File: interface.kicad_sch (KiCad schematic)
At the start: 11 parts, among them J2 USB_C_Receptacle_USB2.0_16P, U2 USBLC6-2P6, U3 FT230XS-R

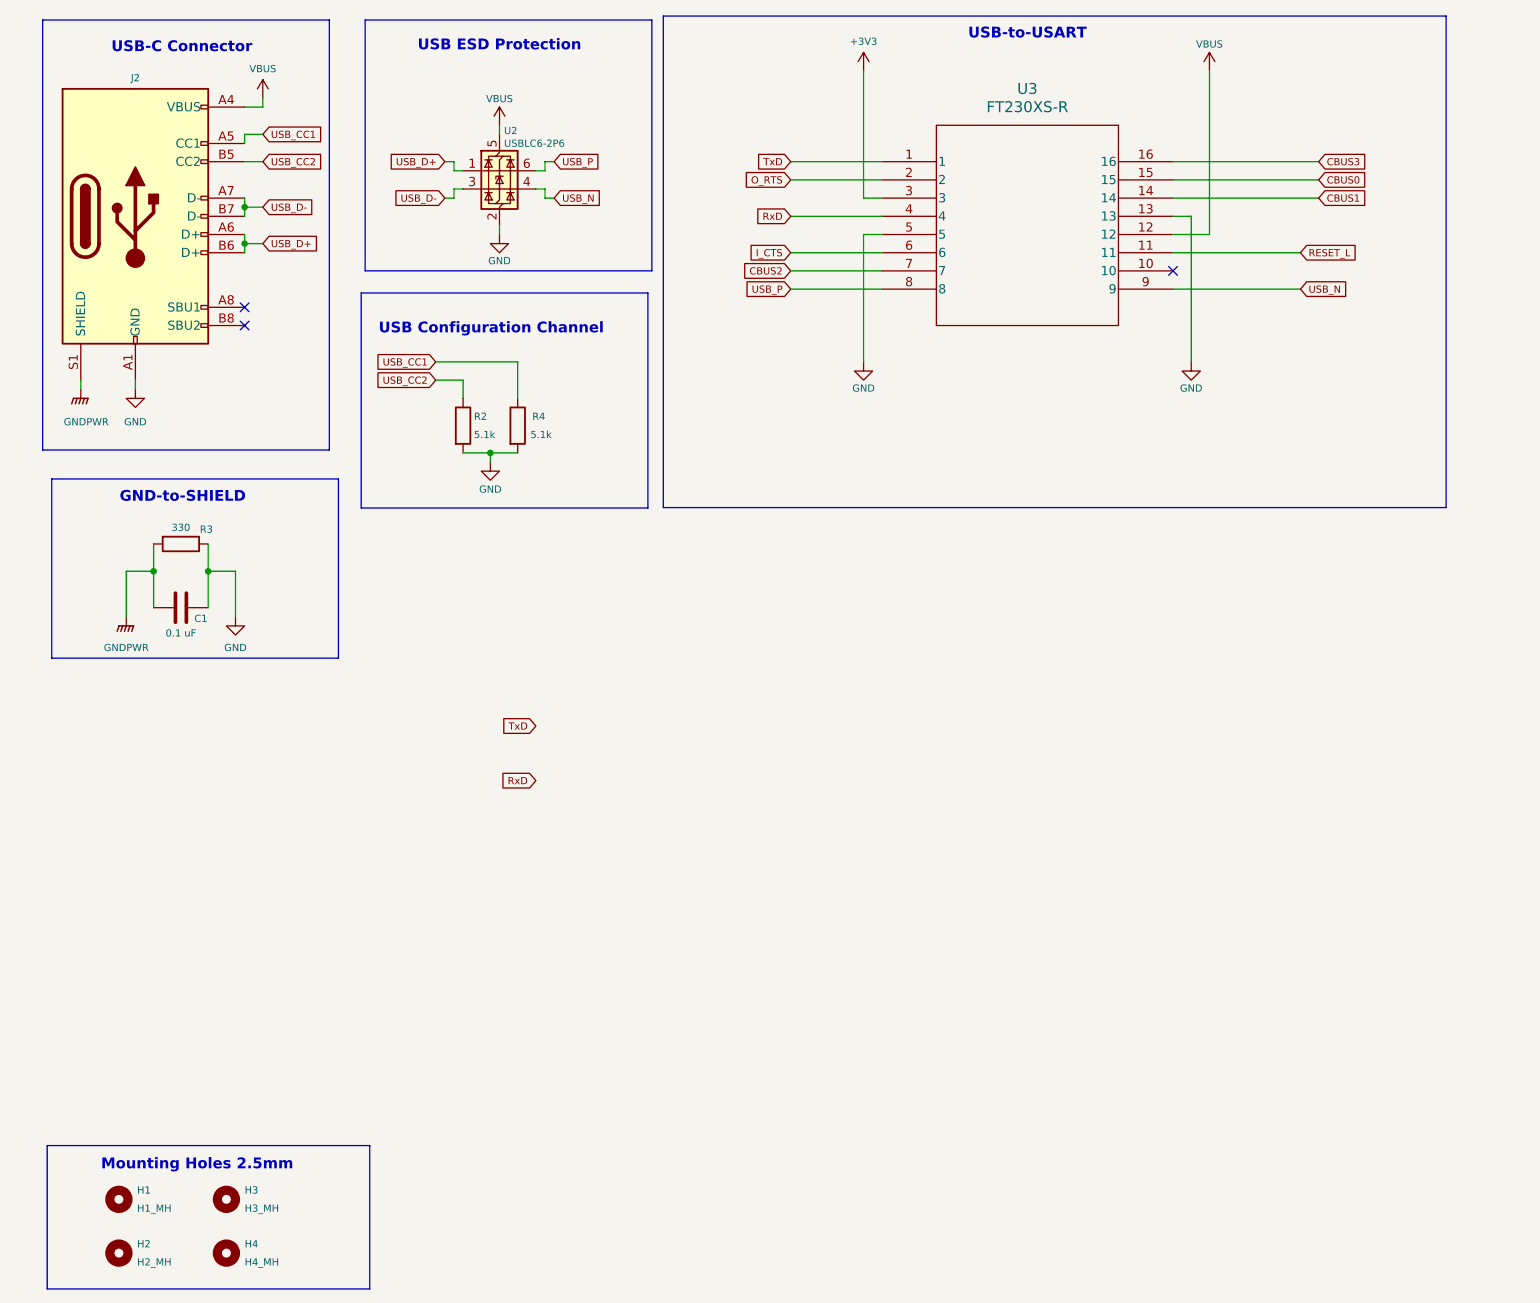
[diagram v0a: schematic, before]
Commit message: finished ERC, matched footprints, populated 3D models
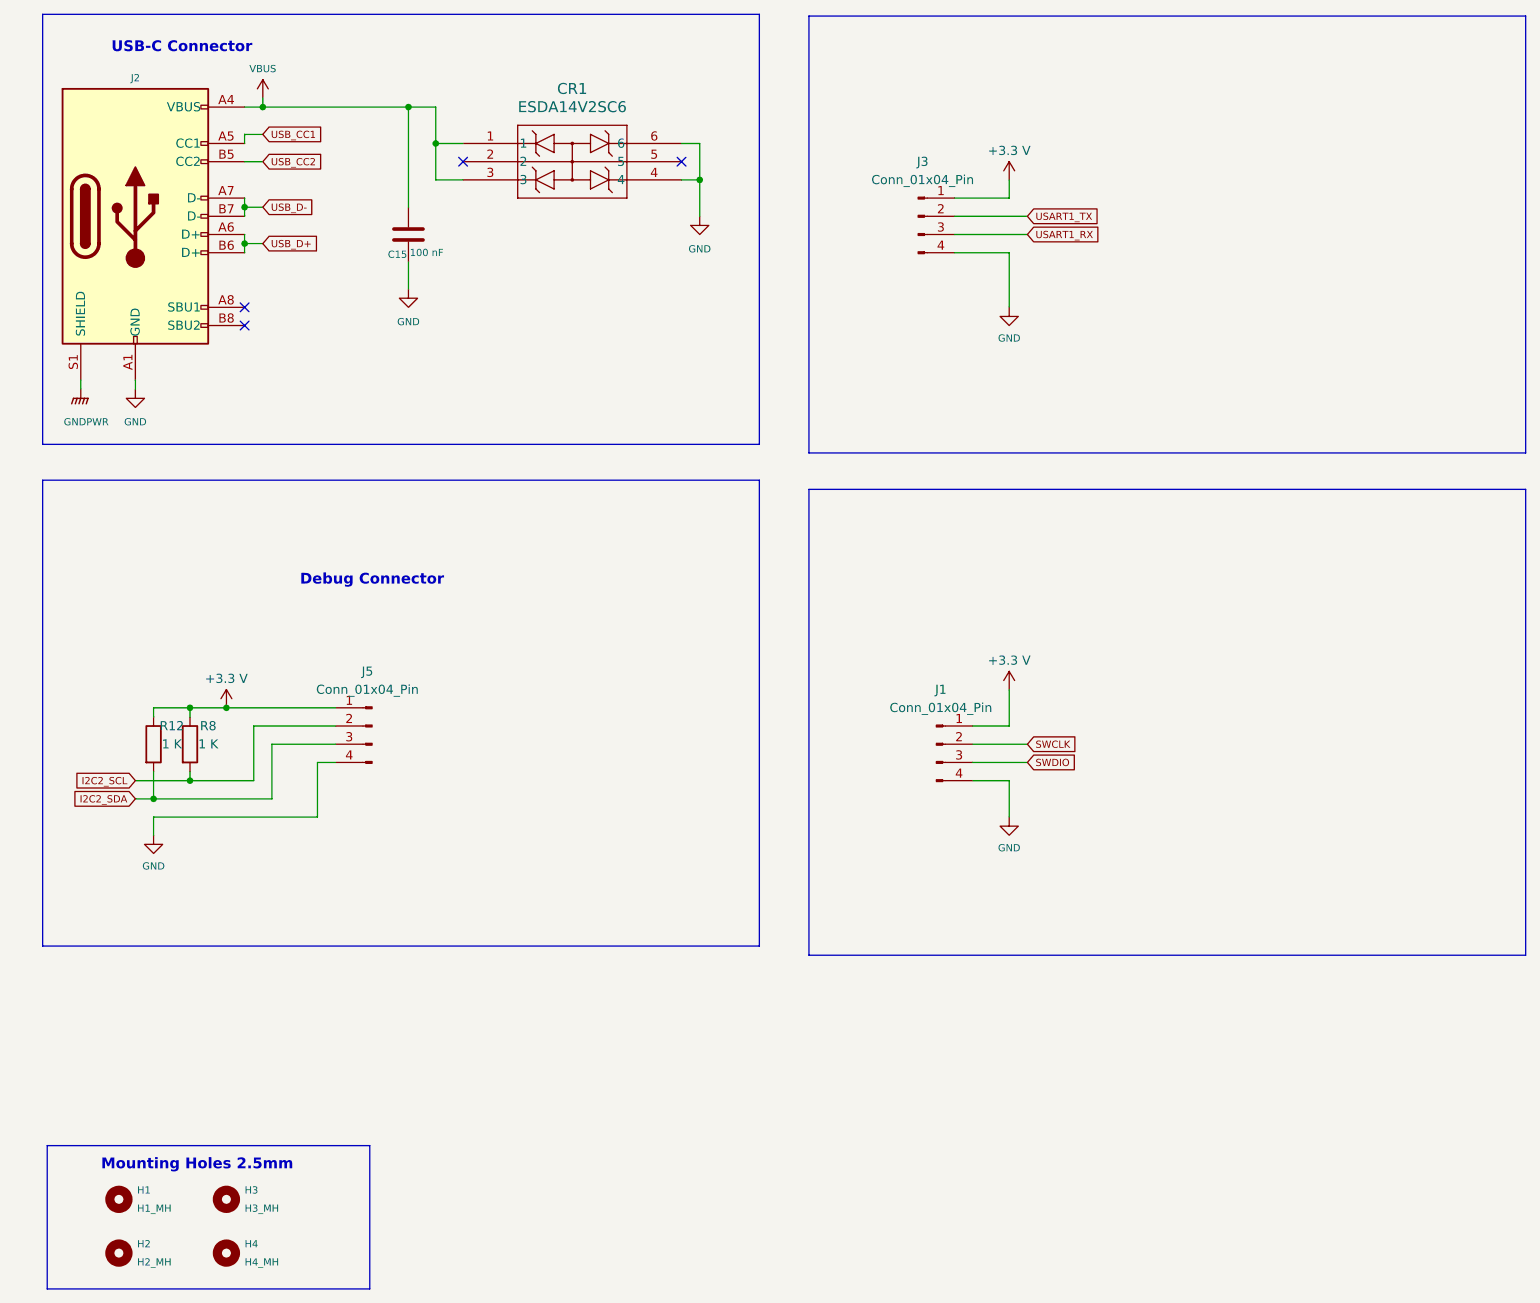
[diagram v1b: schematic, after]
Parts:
- removed C1: 0.1 uF, Capacitor_SMD:C_0805_2012Metric, symbol Device:C
- removed R2, R4: 5.1k, Resistor_SMD:R_0805_2012Metric, symbol Device:R
- removed R3: 330, Resistor_SMD:R_0805_2012Metric, symbol Device:R
- removed U2: USBLC6-2P6, Package_TO_SOT_SMD:SOT-666, symbol Power_Protection:USBLC6-2P6
- removed U3: FT230XS-R, SOIC_30XS-R_FTD, symbol FT230XS-R:FT230XS-R
- added C15: 100 nF, Capacitor_SMD:C_0805_2012Metric, symbol Device:C
- added CR1: ESDA14V2SC6, ESDA14V2SC6:SOT23-6_1P75X3P05X0P95_STM, symbol ESDA14V2SC6:ESDA14V2SC6
- added J1, J3, J5: Conn_01x04_Pin, PPTC041LFBN_RC:SULLINS_PPTC041LFBN-RC, symbol Connector:Conn_01x04_Pin
- added R12, R8: 1 K, Resistor_SMD:R_0805_2012Metric, symbol Device:R
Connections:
- net GND: now also C15.1, CR1.4, CR1.6, J1.4 (Pin_4), J3.4 (Pin_4), J5.4 (Pin_4)
- net VBUS: now also C15.2, CR1.1, CR1.3
- new net +3.3 V: J1.1 (Pin_1), J3.1 (Pin_1), J5.1 (Pin_1), R12.1, R8.1
- new net I2C2_SCL: J5.2 (Pin_2), R8.2
- new net I2C2_SDA: J5.3 (Pin_3), R12.2
- new net SWCLK: J1.2 (Pin_2)
- new net SWDIO: J1.3 (Pin_3)
- new net USART1_RX: J3.3 (Pin_3)
- new net USART1_TX: J3.2 (Pin_2)
- no-connect marks 3 -> 4
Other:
- note added: "Debug Connector"
- note removed: "GND-to-SHIELD"
- note removed: "USB Configuration Channel"
- note removed: "USB ESD Protection"
- note removed: "USB-to-USART"

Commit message: matched footprint name to name of component
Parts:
- J1: footprint PPTC041LFBN_RC:SULLINS_PPTC041LFBN-RC -> PPTC041LFBN_RC:PPTC041LFBN-RC
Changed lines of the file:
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@@
 			)
 		)
-		(property "Footprint" "PPTC041LFBN_RC:SULLINS_PPTC041LFBN-RC"
+		(property "Footprint" "PPTC041LFBN_RC:PPTC041LFBN-RC"
 			(at 139.7 116.84 0)
 			(effects

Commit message: added diode
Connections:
- net +3.3 V: no longer J1.1 (Pin_1), J5.1 (Pin_1), R12.1, R8.1
- new net VBOARD: J5.1 (Pin_1), R12.1, R8.1
- new net VMCU: J1.1 (Pin_1)
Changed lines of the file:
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@@
 	(rectangle
 		(start 121.92 15.24)
-		(end 221.92 76.2)
+		(end 221.92 74.93)
 		(stroke
 			(width 0)
@@
 			)
 		)
-		(property "Value" "+3.3 V"
+		(property "Value" "VBOARD"
 			(at 40.64 107.696 0)
 			(effects
@@
 			)
 		)
-		(property "Value" "+3.3 V"
+		(property "Value" "VMCU"
 			(at 149.86 105.156 0)
 			(effects

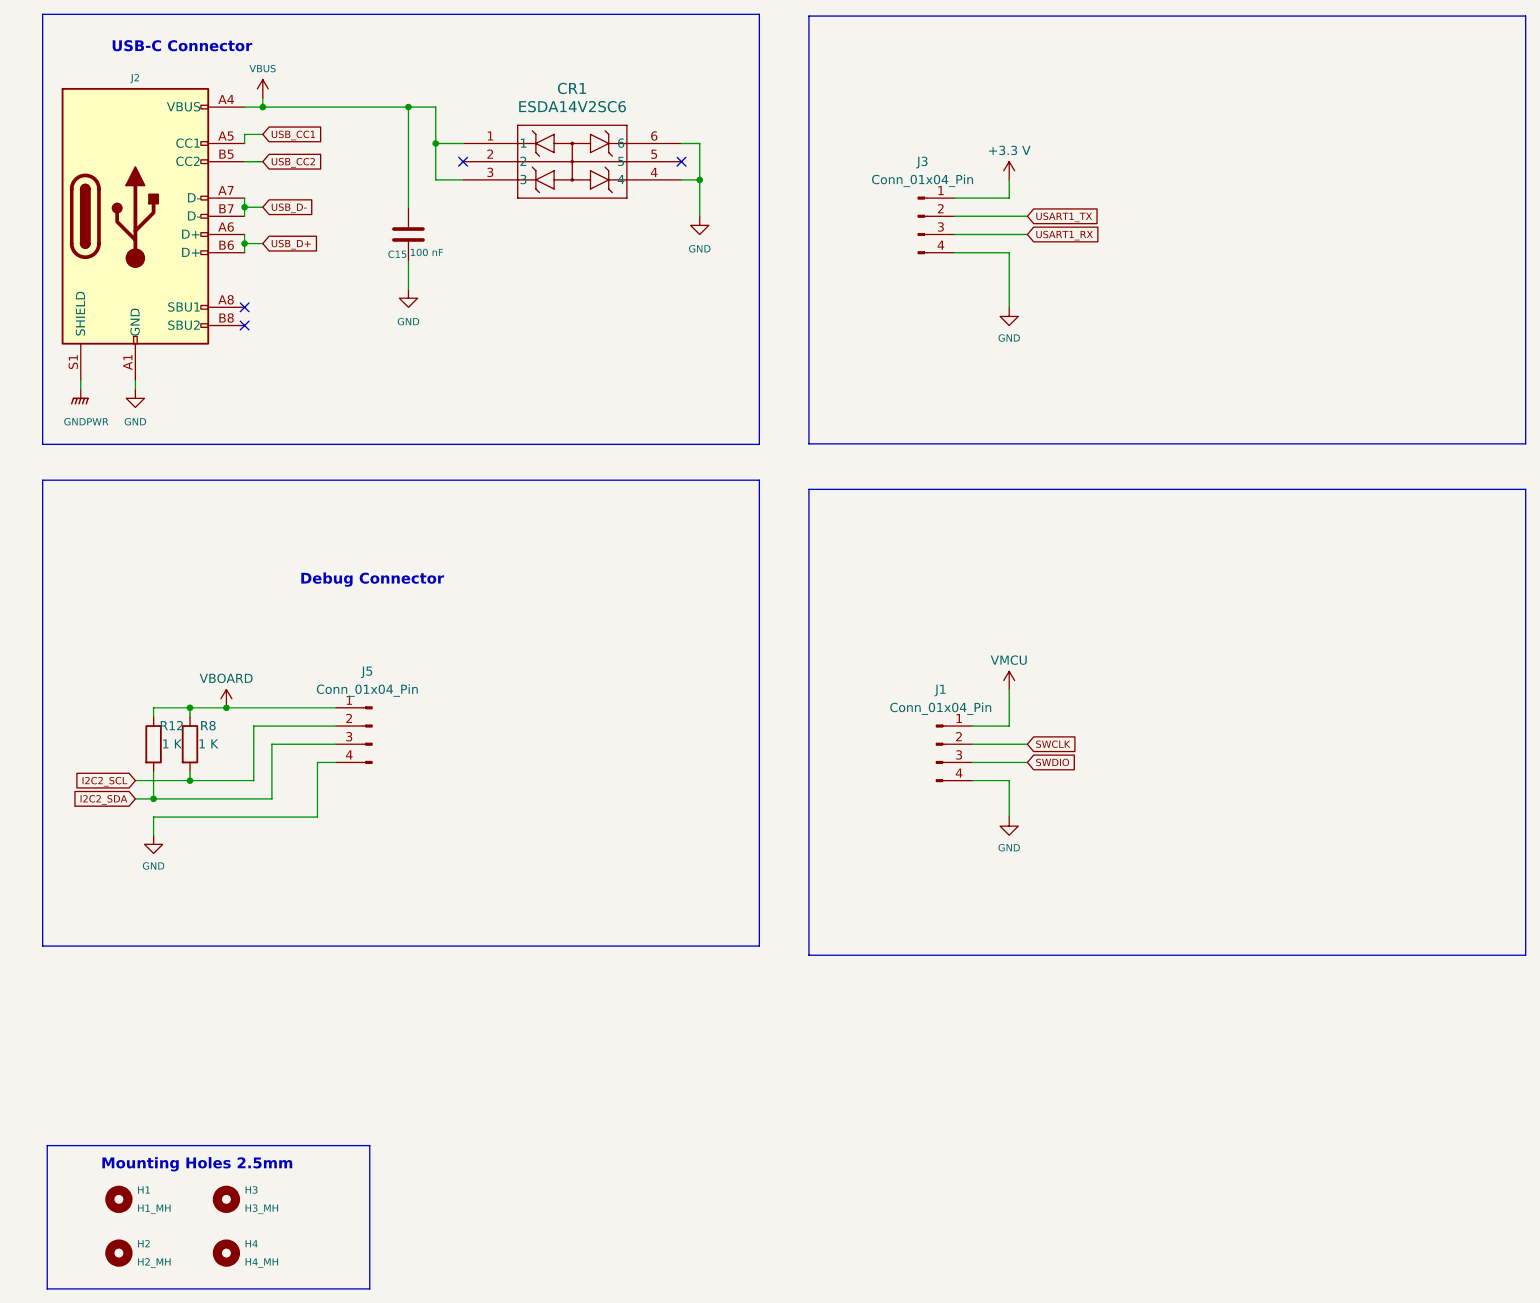
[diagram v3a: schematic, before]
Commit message: separated voltage source labels
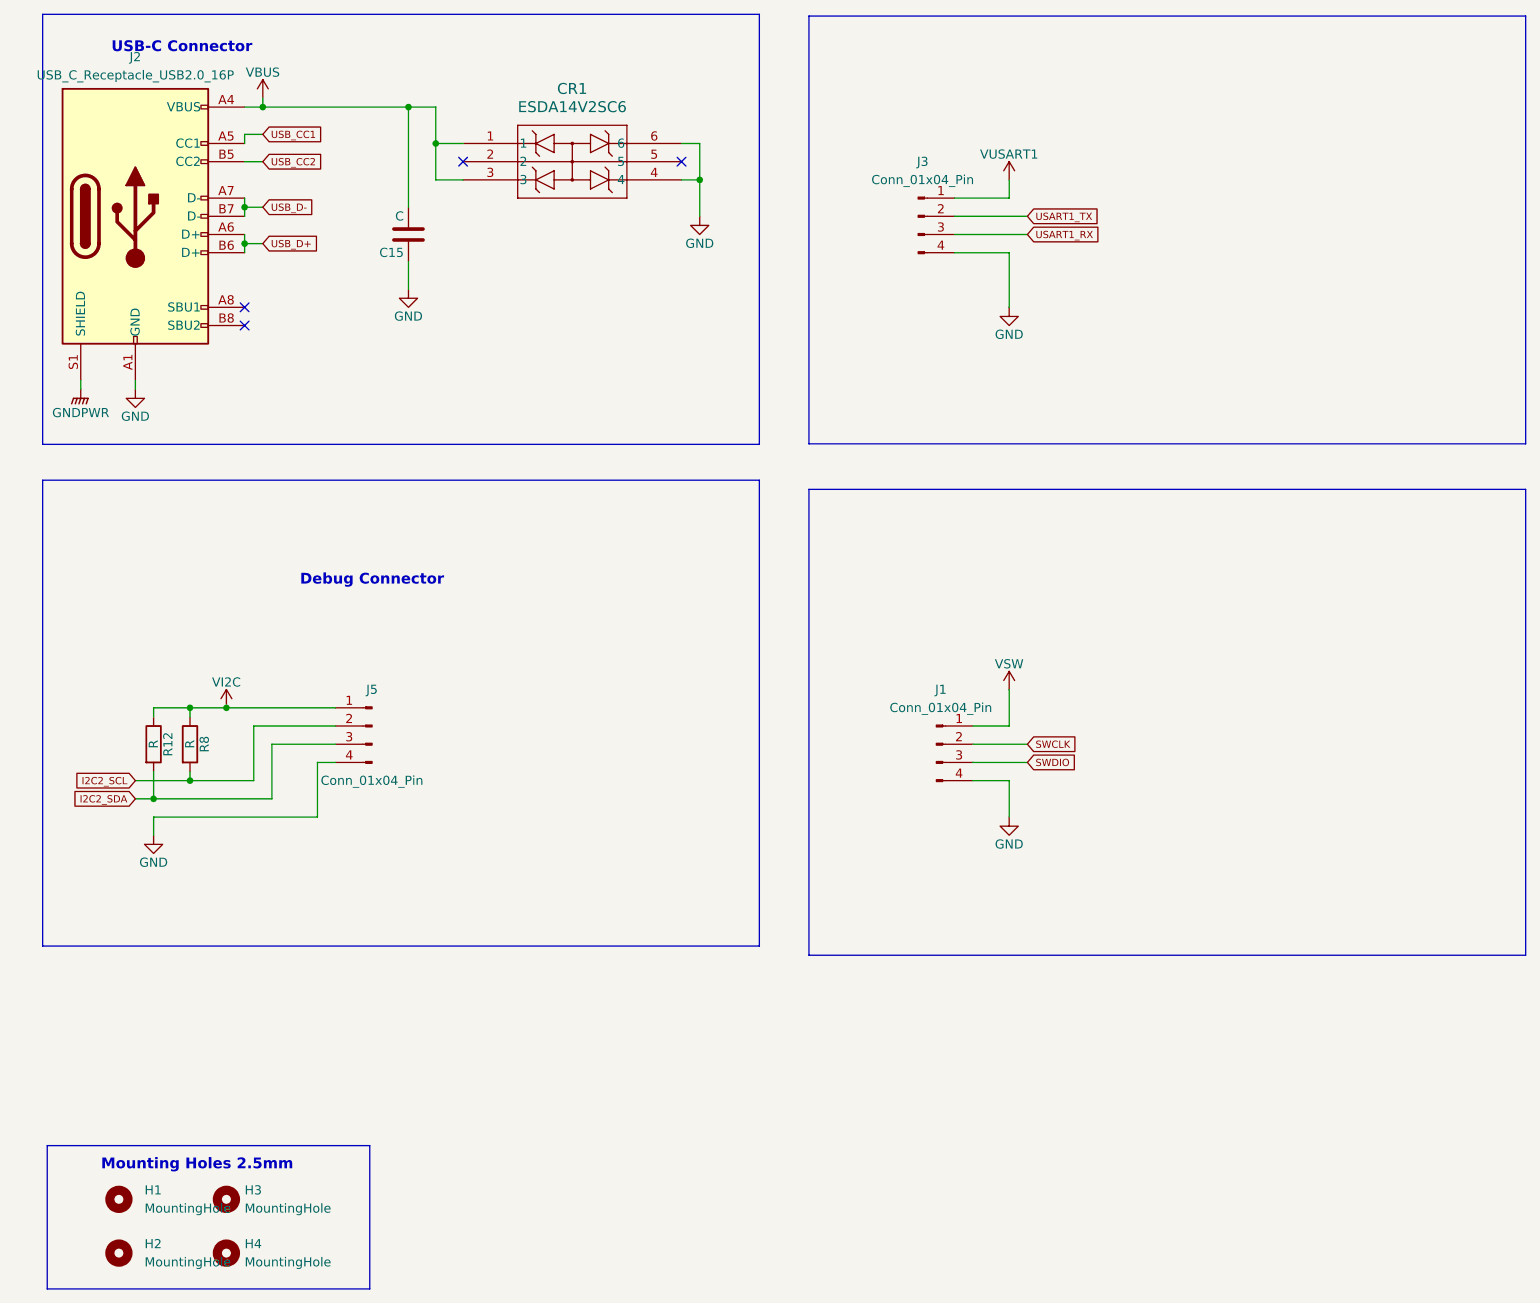
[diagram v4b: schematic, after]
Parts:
- C15: value 100 nF -> C
- H1: value H1_MH -> MountingHole
- H2: value H2_MH -> MountingHole
- H3: value H3_MH -> MountingHole
- H4: value H4_MH -> MountingHole
- R12, R8: value 1 K -> R
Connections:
- net +3.3 V renamed VUSART1
- net VBOARD renamed VI2C
- net VMCU renamed VSW
